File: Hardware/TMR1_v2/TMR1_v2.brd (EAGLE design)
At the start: 34.3 x 34.3 mm, 47 parts, among them U1 ATMEGA328P_TQFP, U2 MCP79410I/SN, Y1 32.768kHz

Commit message: std easy schematic with all elements in board before route
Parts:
- removed R17: 4.7k, SparkFun-Resistors:0402
- removed S2: MOMENTARY-SWITCH-SPST-SMD-RIGHT-ANGLE, SparkFun-Switches:TACTILE_SWITCH_SMD_RIGHT_ANGLE
- added R15: 10k, SparkFun-Resistors:0603
- added S1: MOMENTARY-SWITCH-SPST-SMD-5.2MM, SparkFun-Switches:TACTILE_SWITCH_SMD_5.2MM
- added TP11, TP12: TEST-POINT3X4, SparkFun-Connectors:PAD.03X.04
- C2, C4: value 6.8pF -> 22pF; device SparkFun-Capacitors:0402 -> SparkFun-Capacitors:0603
- C3: value 10uF -> 100nF
- D1, D10, D11, D12, D2, D3, D4, D5, D6, D7, D8, D9: device standardparts:0402.LED -> SparkFun-LED:LED-0603
- R1, R10, R11, R12, R2, R3, R4, R5, R6, R7, R8, R9: value 200 -> 330; device SparkFun-Resistors:0402 -> SparkFun-Resistors:0603
- R13, R14: device SparkFun-Resistors:0402 -> SparkFun-Resistors:0603
- R16: value 4.7k -> 10k; device SparkFun-Resistors:0402 -> SparkFun-Resistors:0603
- moved R10 44.9 mm to (12.7, 38.1), turned to 225 degrees
- moved R9 43.3 mm to (10.2, 29.2), turned to 270 degrees
- moved D9 42.2 mm to (7.62, 25.4), turned to 270 degrees
- moved R8 42.2 mm to (10.2, 21.6), turned to 270 degrees
- moved D8 42.0 mm to (10.2, 16.5), turned to 288.5 degrees
- moved R11 41.6 mm to (20.3, 41.9), turned to 206.5 degrees
- moved R7 39.9 mm to (12.7, 12.7), turned to 315 degrees
- moved D10 39.9 mm to (10.2, 34.3), turned to 243.5 degrees
- moved D7 39.6 mm to (16.5, 10.2), turned to 333.5 degrees
- moved C3 37.4 mm to (16.5, 16.5), flipped to the bottom, turned to 225 degrees
- moved R12 36.7 mm to (30.5, 41.9), turned to 153.5 degrees
- moved D11 36.0 mm to (16.5, 40.6), turned to 225 degrees
- moved D6 34.9 mm to (25.4, 7.62)
- moved R6 34.3 mm to (20.3, 7.62)
- moved C2 33.0 mm to (15.2, 35.6), turned to 45 degrees
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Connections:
- net D1: now also R1.1; no longer R1.2
- net D10: now also R10.1; no longer R10.2
- net D11: now also R11.1; no longer R11.2
- net D12: now also R12.1; no longer R12.2
- net D2: now also R2.1; no longer R2.2
- net D3: now also R3.1; no longer R3.2
- net D4: now also R4.1; no longer R4.2
- net D5: now also R5.1; no longer R5.2
- net D6: now also R6.1; no longer R6.2
- net D7: now also R7.1; no longer R7.2
- net D8: now also R8.1; no longer R8.2
- net D9: now also R9.1; no longer R9.2
- net GND: now also C2.1, C4.1, D1.C, D10.C, D11.C, D12.C, D2.C, D3.C, D4.C, D5.C, D6.C, D7.C, D8.C, D9.C, R15.1, TP12.P$1; no longer C2.2, C4.2, D1.P$2, D10.P$2, D11.P$2, D12.P$2, D2.P$2, D3.P$2, D4.P$2, D5.P$2, D6.P$2, D7.P$2, D8.P$2, D9.P$2, R14.2
- net MISO: now also TP7.P$1; no longer TP8.P$1
- net MOSI: now also TP10.P$1; no longer TP9.P$1
- net N$1: now also D8.A, R8.2; no longer D8.P$1, R8.1
- net N$10: now also C4.2; no longer C2.1
- net N$18: now also D9.A, R9.2; no longer D9.P$1, R9.1
- net N$2: now also D7.A, R7.2; no longer D7.P$1, R7.1
- net N$20: now also D10.A, R10.2; no longer D10.P$1, R10.1
- net N$22: now also D11.A, R11.2; no longer D11.P$1, R11.1
- net N$24: now also D12.A, R12.2; no longer D12.P$1, R12.1
- net N$3: now also D6.A, R6.2; no longer D6.P$1, R6.1
- net N$4: now also D5.A, R5.2; no longer D5.P$1, R5.1
- net N$5: now also D4.A, R4.2; no longer D4.P$1, R4.1
- net N$6: now also D3.A, R3.2; no longer D3.P$1, R3.1
- net N$7: now also D2.A, R2.2; no longer D2.P$1, R2.1
- net N$8: now also D1.A, R1.2; no longer D1.P$1, R1.1
- net N$9: now also C2.2; no longer C4.1
- net PUSH: now also R15.2, S1.3; no longer R14.1, S2.2
- net RST: now also R16.1, TP11.P$1; no longer R13.2, TP10.P$1
- net SCK: now also TP9.P$1; no longer TP7.P$1
- net SCL: now also R13.1; no longer R17.2
- net SDA: now also R14.1; no longer R16.2
- net VCC: now also R13.2, R14.2, R16.2, S1.1, TP8.P$1; no longer R13.1, R16.1, R17.1, S2.1
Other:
- board size 34.3 x 34.3 mm -> 100 x 80 mm

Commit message: before routing
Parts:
- added J1, J2: 455-1750-1-ND, SparkFun-Connectors:1X03
- added J3, J4: (no value), SparkFun-Connectors:1X04
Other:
- board size 100 x 80 mm -> 41 x 48.3 mm
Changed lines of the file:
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@@
 <board>
 <plain>
-<wire x1="0" y1="0" x2="100" y2="0" width="0" layer="20"/>
-<wire x1="100" y1="0" x2="100" y2="80" width="0" layer="20"/>
-<wire x1="100" y1="80" x2="0" y2="80" width="0" layer="20"/>
-<wire x1="0" y1="80" x2="0" y2="0" width="0" layer="20"/>
-<circle x="25.4" y="25.4" radius="20.478134375" width="0.1524" layer="46"/>
-<wire x1="5.08" y1="25.4" x2="25.4" y2="25.4" width="0.1524" layer="46"/>
-<wire x1="25.4" y1="25.4" x2="45.72" y2="25.4" width="0.1524" layer="46"/>
-<wire x1="25.4" y1="5.08" x2="25.4" y2="25.4" width="0.1524" layer="46"/>
-<wire x1="25.4" y1="25.4" x2="25.4" y2="45.72" width="0.1524" layer="46"/>
-<wire x1="25.4" y1="25.4" x2="40.64" y2="40.64" width="0.1524" layer="46"/>
-<wire x1="25.4" y1="25.4" x2="10.16" y2="10.16" width="0.1524" layer="46"/>
-<wire x1="25.4" y1="25.4" x2="40.64" y2="10.16" width="0.1524" layer="46"/>
-<wire x1="25.4" y1="25.4" x2="10.16" y2="40.64" width="0.1524" layer="46"/>
-<circle x="25.4" y="25.4" radius="17.78" width="0.1524" layer="46"/>
+<wire x1="35.56" y1="43.18" x2="35.56" y2="7.62" width="0.1524" layer="20" curve="-120.510237"/>
+<wire x1="15.24" y1="7.62" x2="15.24" y2="43.18" width="0.1524" layer="20" curve="-120.510237"/>
+<wire x1="15.24" y1="7.62" x2="15.24" y2="1.27" width="0.1524" layer="20"/>
+<wire x1="15.24" y1="1.27" x2="35.56" y2="1.27" width="0.1524" layer="20"/>
+<wire x1="35.56" y1="1.27" x2="35.56" y2="7.62" width="0.1524" layer="20"/>
+<wire x1="15.24" y1="43.18" x2="15.24" y2="49.53" width="0.1524" layer="20"/>
+<wire x1="15.24" y1="49.53" x2="35.56" y2="49.53" width="0.1524" layer="20"/>
+<wire x1="35.56" y1="49.53" x2="35.56" y2="43.18" width="0.1524" layer="20"/>
 </plain>
 <attributes>
@@
 <element name="TP11" library="SparkFun-Connectors" package="PAD.03X.04" value="TEST-POINT3X4" x="11.43" y="27.94" rot="MR0"/>
 <element name="TP12" library="SparkFun-Connectors" package="PAD.03X.04" value="TEST-POINT3X4" x="13.97" y="27.94" rot="MR0"/>
+<element name="J1" library="SparkFun-Connectors" package="1X03" value="455-1750-1-ND" x="27.94" y="46.99">
+<attribute name="NAME" x="26.67" y="48.387" size="0.6096" layer="25" font="vector" ratio="20"/>
+<attribute name="PROD_ID" value="XXX-00000" x="27.94" y="46.99" size="1.778" layer="27" display="off"/>
+<attribute name="VALUE" x="26.67" y="44.958" size="0.6096" layer="27" font="vector" ratio="20"/>
+</element>
+<element name="J2" library="SparkFun-Connectors" package="1X03" value="455-1750-1-ND" x="27.94" y="3.81">
+<attribute name="NAME" x="26.67" y="5.207" size="0.6096" layer="25" font="vector" ratio="20"/>
+<attribute name="PROD_ID" value="XXX-00000" x="27.94" y="3.81" size="1.778" layer="27" display="off"/>
+<attribute name="VALUE" x="26.67" y="1.778" size="0.6096" layer="27" font="vector" ratio="20"/>
+</element>
+<element name="J3" library="SparkFun-Connectors" package="1X04" value="" x="17.78" y="3.81">
+<attribute name="NAME" x="16.51" y="5.207" size="0.6096" layer="25" font="vector" ratio="20"/>
+<attribute name="PROD_ID" value="CONN-09696" x="17.78" y="3.81" size="1.778" layer="27" display="off"/>
+<attribute name="VALUE" x="16.51" y="1.778" size="0.6096" layer="27" font="vector" ratio="20"/>
+</element>
+<element name="J4" library="SparkFun-Connectors" package="1X04" value="" x="17.78" y="46.99">
+<attribute name="NAME" x="16.51" y="48.387" size="0.6096" layer="25" font="vector" ratio="20"/>
+<attribute name="PROD_ID" value="CONN-09696" x="17.78" y="46.99" size="1.778" layer="27" display="off"/>
+<attribute name="VALUE" x="16.51" y="44.958" size="0.6096" layer="27" font="vector" ratio="20"/>
+</element>
 </elements>
 <signals>

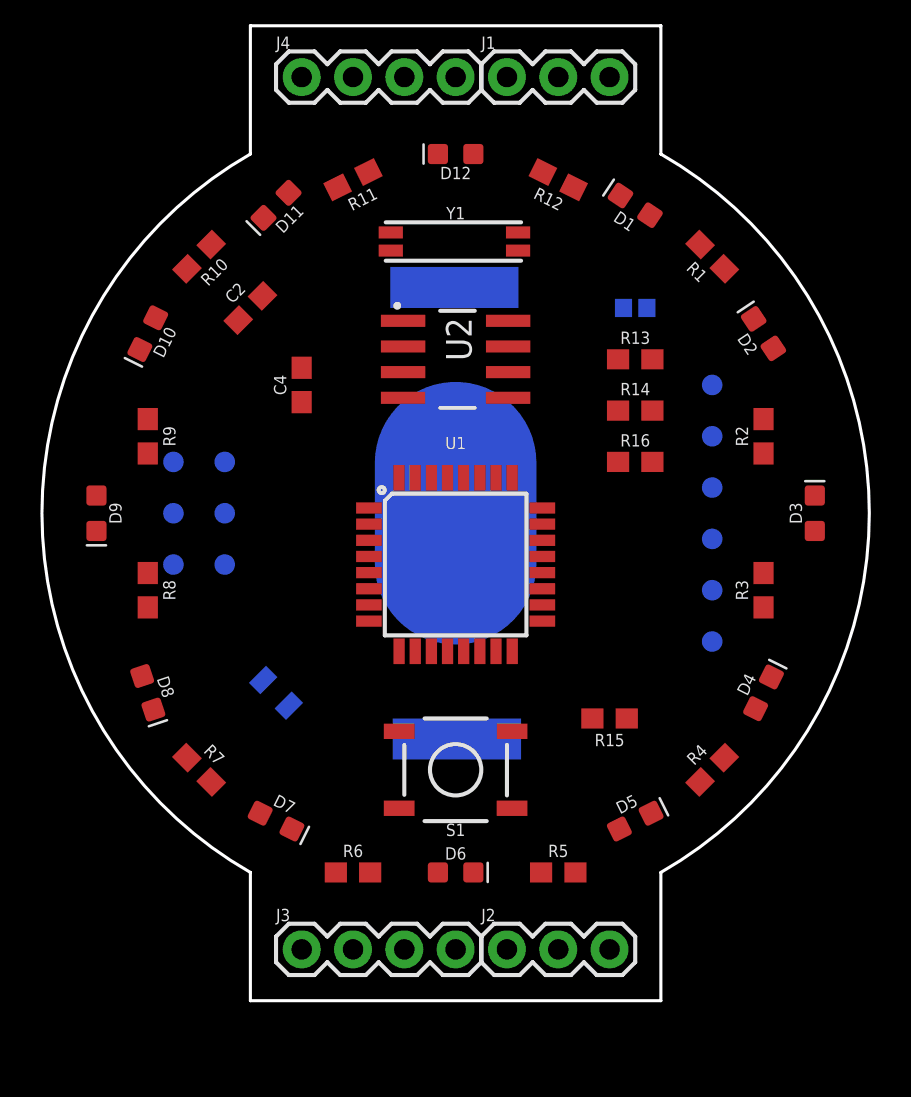
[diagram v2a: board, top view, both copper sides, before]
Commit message: we may not need RX and TX
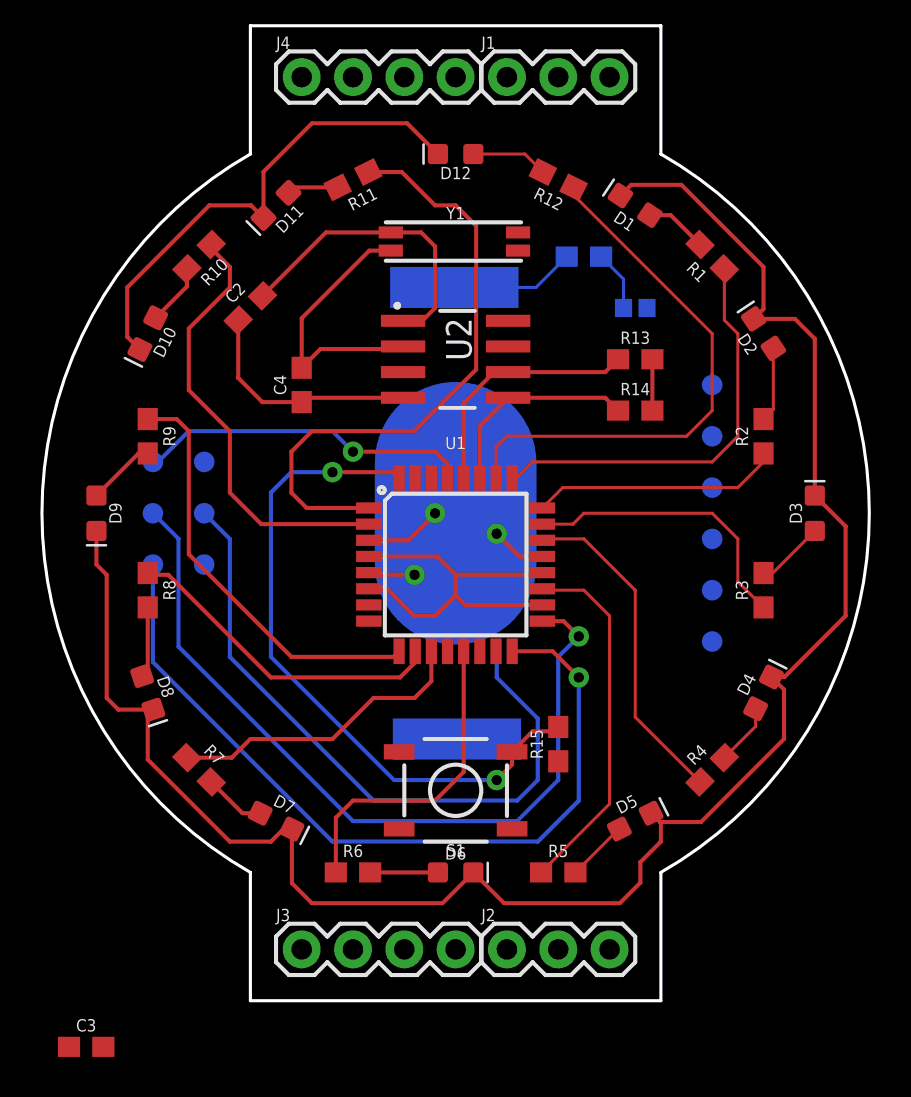
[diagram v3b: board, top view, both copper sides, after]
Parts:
- C3: device SparkFun-Capacitors:0805 -> SparkFun-Capacitors:0603
- moved C3 19.9 mm to (7.11, -1.02), flipped to the top, turned to 0 degrees
- moved R16 10.5 mm to (31.8, 38.1), flipped to the bottom
- moved R15 2.84 mm to (30.5, 14.0), turned to 90 degrees
- moved S1 1.02 mm to (25.4, 11.7)
- moved TP10 1.02 mm to (13.0, 25.4)
- moved TP11 1.02 mm to (10.4, 27.9)
- moved TP12 1.02 mm to (13.0, 27.9)
- moved TP7 1.02 mm to (10.4, 22.9)
- moved TP8 1.02 mm to (13.0, 22.9)
- moved TP9 1.02 mm to (10.4, 25.4)
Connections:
- net GND: now also C3.2; no longer C3.1
- net VCC: now also C3.1; no longer C3.2
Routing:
- net GND: track 0.00 -> 147.2 mm, vias 0 -> 3
- net MISO: track 0.00 -> 40.4 mm, vias 0 -> 1
- net SCK: track 0.00 -> 40.0 mm, vias 0 -> 1
- net PUSH: track 0.00 -> 33.2 mm, vias 0 -> 2
- net MOSI: track 0.00 -> 33.2 mm
- net D11: track 0.00 -> 30.6 mm
- net VCC: track 0.00 -> 26.9 mm
- net D12: track 0.00 -> 26.9 mm
- net D10: track 0.00 -> 21.9 mm
- net D9: track 0.00 -> 21.0 mm
- net D1: track 0.00 -> 20.6 mm
- net RST: track 0.00 -> 19.6 mm, vias 0 -> 1
- net D5: track 0.00 -> 18.0 mm
- net D4: track 0.00 -> 16.5 mm
- net D8: track 0.00 -> 16.2 mm
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
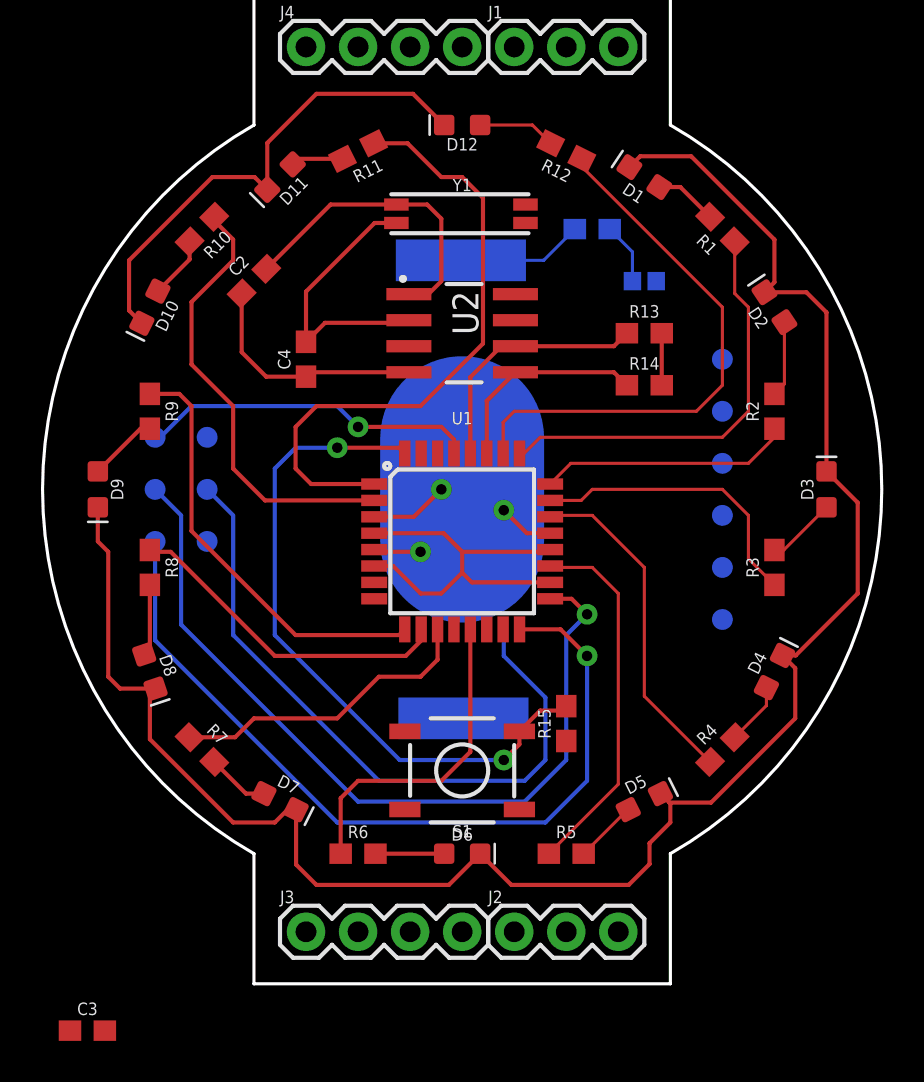
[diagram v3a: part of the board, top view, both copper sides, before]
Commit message: PCB finished and Gerbers generated
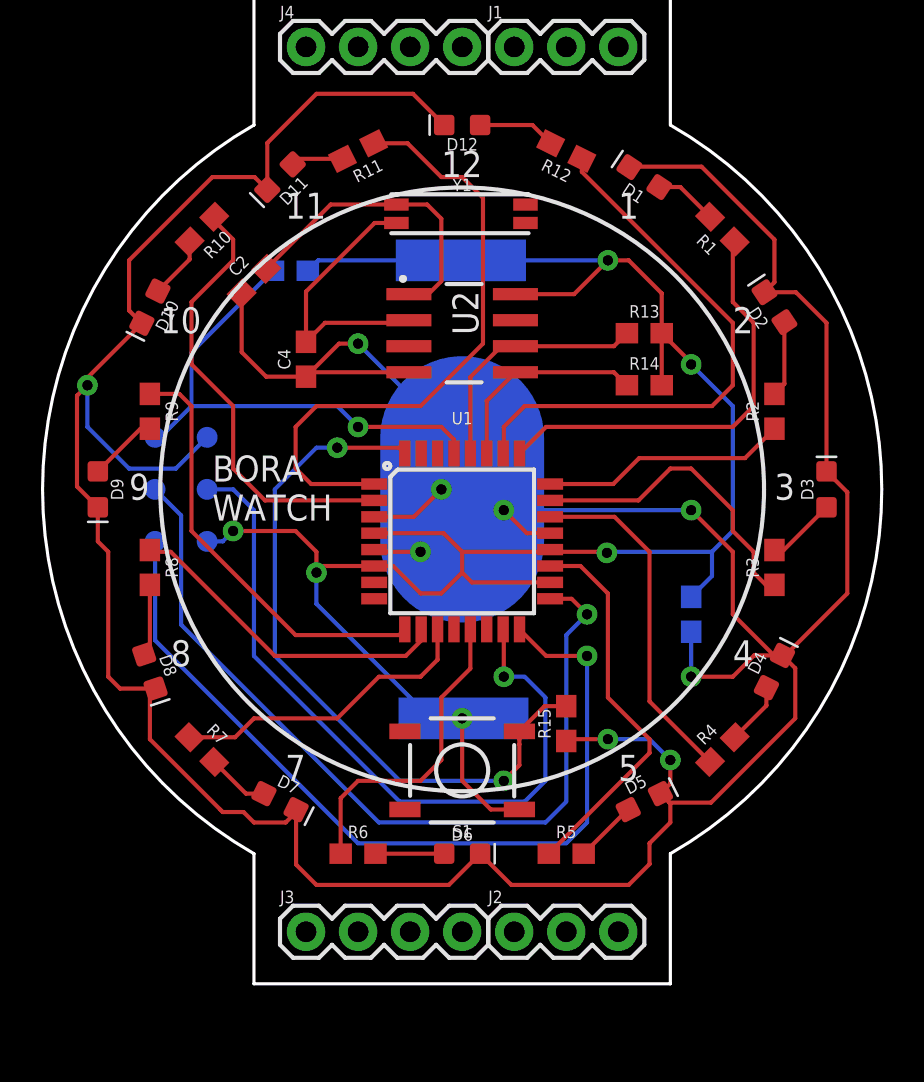
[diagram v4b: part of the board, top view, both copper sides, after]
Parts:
- removed C1: 0.1uF, SparkFun-Capacitors:0402
- removed TP1, TP2, TP3, TP4, TP5, TP6: TEST-POINT3X4, SparkFun-Connectors:PAD.03X.04
- moved C3 35.8 mm to (36.6, 19.3), flipped to the bottom, turned to 270 degrees
- moved R16 14.9 mm to (17.0, 36.1), turned to 180 degrees
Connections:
- removed net DTR: C1.1, TP6.P$1
- net GND: no longer TP1.P$1, TP2.P$1
- net RST: no longer C1.2
- net RX: no longer TP4.P$1
- net TX: no longer TP5.P$1
- net VCC: no longer TP3.P$1
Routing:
- net VCC: track 26.9 -> 99.8 mm, vias 0 -> 6
- net GND: track 147.2 -> 210.6 mm, vias 3 -> 9
- net RST: track 19.6 -> 24.8 mm
- net MOSI: track 33.2 -> 36.3 mm, vias 0 -> 1
- net SCK: track 40.0 -> 42.0 mm
- net MISO: track 40.4 -> 42.4 mm
- net PUSH: track 33.2 -> 34.7 mm
- net D5: track 18.0 -> 19.0 mm
- net D3: track 14.3 -> 15.1 mm
- net D6: track 16.0 -> 15.4 mm
- net DTR: track 0.58 -> 0.00 mm
- net D12: track 26.9 -> 27.4 mm
- net D4: track 16.5 -> 17.0 mm
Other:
- board text added: "1"
- board text added: "10"
- board text added: "11"
- board text added: "12"
- board text added: "2"
- board text added: "3"
- board text added: "4"
- board text added: "5"
- board text added: "7"
- board text added: "8"
- board text added: "9"
- board text added: "AHERRERO"
- board text added: "BORA WATCH"
